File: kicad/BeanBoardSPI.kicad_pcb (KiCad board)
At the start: 4 copper layers, 199.4 x 80 mm, 42 parts, among them J1 Conn_01x16_Pin, J10 SPI1, J11 SPI2, J12 SPI3, J13 SPI4, J14 SPI5, J15 SPI6, J2 Conn_01x16_Pin, J3 Conn_01x03_Pin, J4 Conn_01x10_Pin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

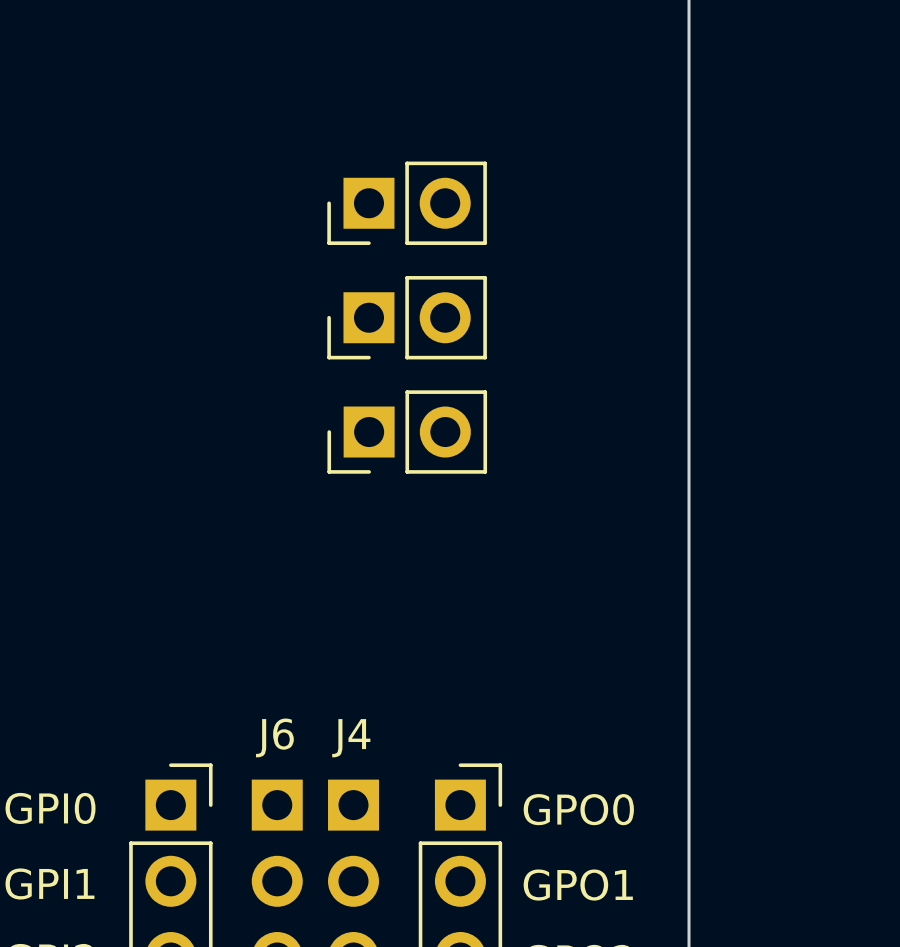
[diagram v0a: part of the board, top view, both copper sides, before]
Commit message: layout / schematic
clock divider labelling
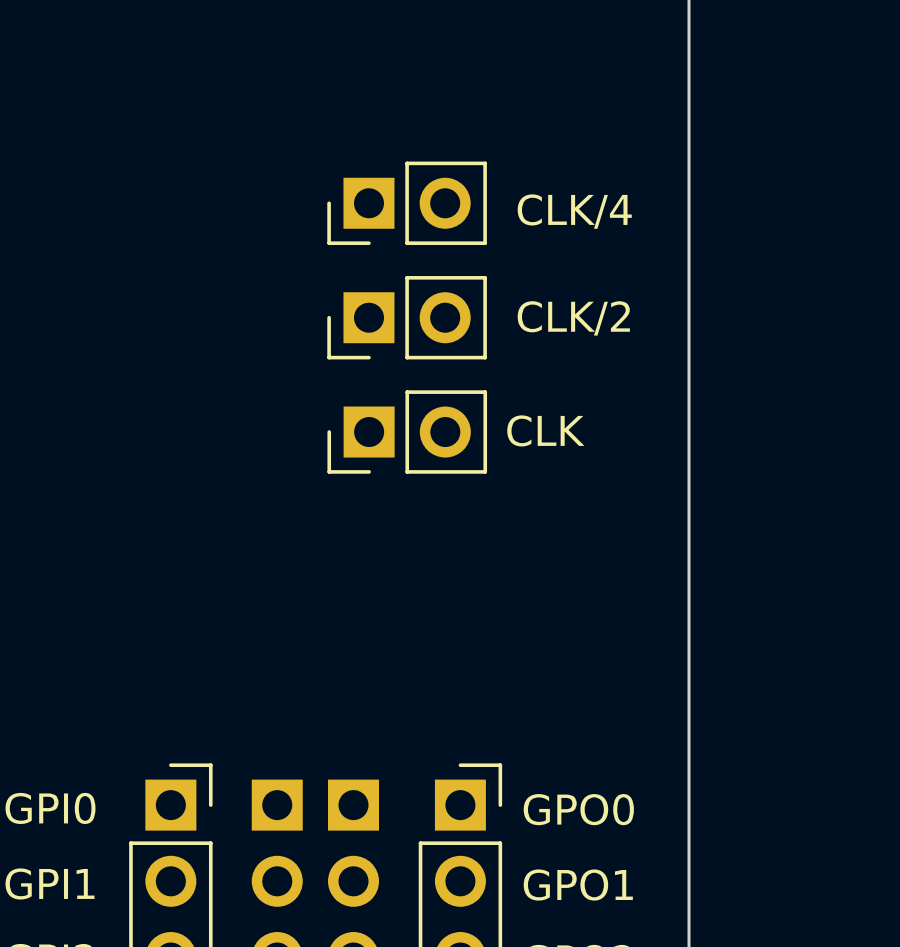
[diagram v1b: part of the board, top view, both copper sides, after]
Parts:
- JP1: value Jumper_2_Open -> CLK
- JP2: value Jumper_2_Open -> CLK/2
- JP3: value Jumper_2_Bridged -> CLK/4
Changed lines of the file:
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@@
 			)
 		)
-		(property "Value" "Jumper_2_Open"
+		(property "Value" "CLK/2"
 			(at -0.005 6.858 180)
-			(layer "F.Fab")
+			(layer "F.SilkS")
 			(effects
 				(font
@@
 		(property "Reference" "J4"
 			(at 0 -2.33 0)
-			(layer "F.SilkS")
+			(layer "F.Fab")
 			(effects
 				(font
@@
 		(property "Reference" "J6"
 			(at 0 -2.33 0)
-			(layer "F.SilkS")
+			(layer "F.Fab")
 			(effects
 				(font
@@
 			)
 		)
-		(property "Value" "Jumper_2_Open"
+		(property "Value" "CLK"
 			(at 0 5.837 180)
-			(layer "F.Fab")
+			(layer "F.SilkS")
 			(effects
 				(font
@@
 			)
 		)
-		(property "Value" "Jumper_2_Bridged"
+		(property "Value" "CLK/4"
 			(at -0.259 6.858 180)
-			(layer "F.Fab")
+			(layer "F.SilkS")
 			(effects
 				(font

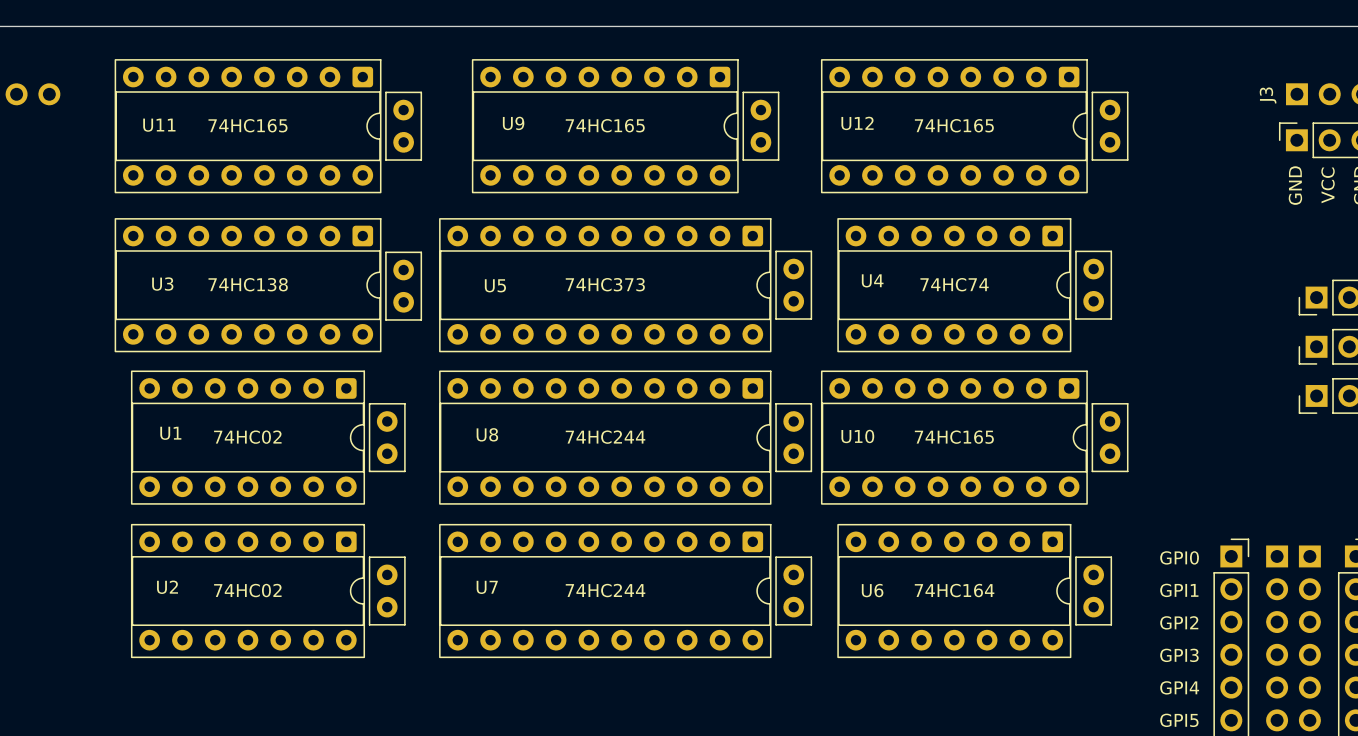
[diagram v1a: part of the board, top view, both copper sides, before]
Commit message: Update BeanBoardSPI.kicad_pcb
cap positioning
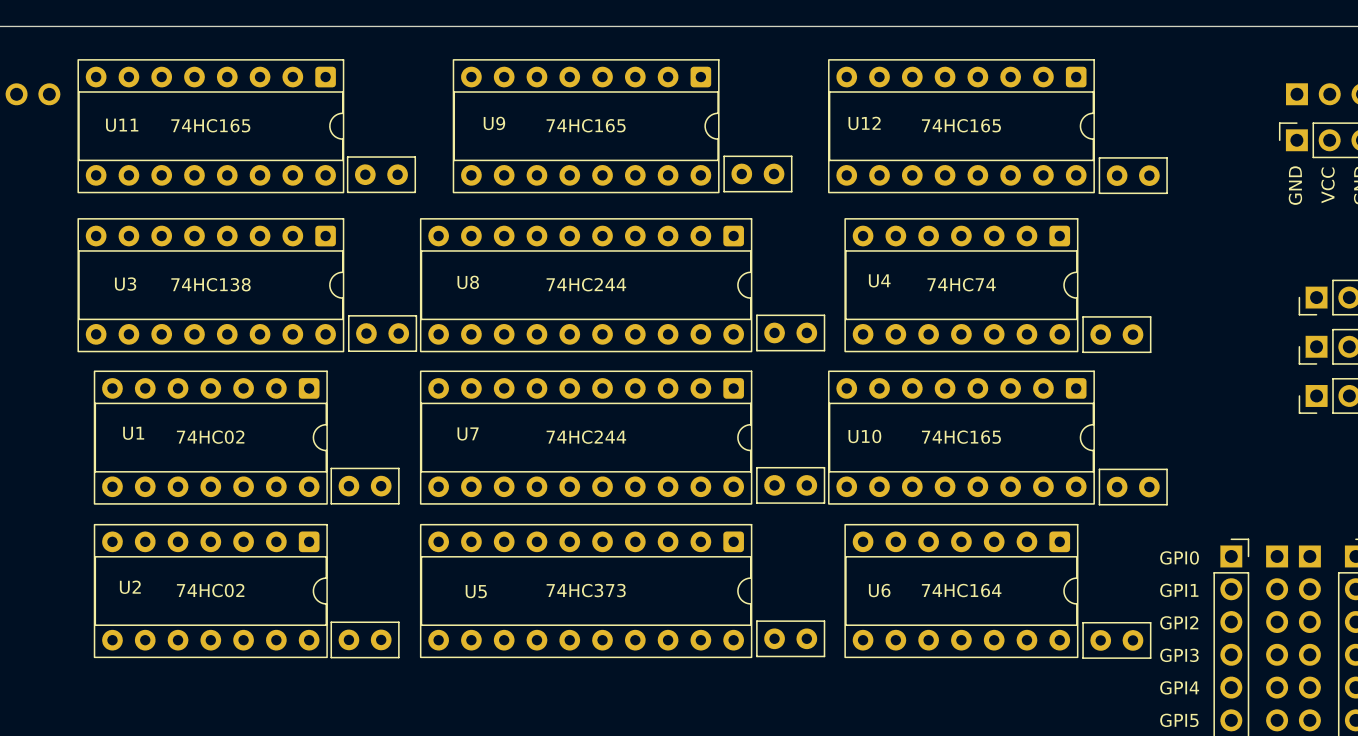
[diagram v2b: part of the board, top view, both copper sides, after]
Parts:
- moved U5 23.7 mm to (245.2, 54.7)
- moved U7 12.0 mm to (245.2, 42.8)
- moved U8 11.9 mm to (245.2, 31.0)
- moved C5 5.82 mm to (216.6, 26.2), turned to 0 degrees
- moved C6 5.70 mm to (216.7, 38.5), turned to 0 degrees
- moved C3 5.17 mm to (245.8, 26.2), turned to 0 degrees
- moved C10 5.17 mm to (248.3, 50.3), turned to 0 degrees
- moved C4 5.17 mm to (248.3, 62.2), turned to 0 degrees
- moved C9 5.17 mm to (248.3, 38.5), turned to 0 degrees
- moved C2 5.11 mm to (274.9, 50.4), turned to 0 degrees
- moved C7 5.11 mm to (273.6, 38.6), turned to 0 degrees
- moved C1 5.11 mm to (274.9, 26.3), turned to 0 degrees
- moved C8 5.11 mm to (273.6, 62.3), turned to 0 degrees
- moved U1 2.88 mm to (212.3, 42.8)
- moved U11 2.88 mm to (213.5, 18.7)
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
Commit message: Update BeanBoardSPI.kicad_pcb
tracks - data
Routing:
- net /D5: track 0.00 -> 109.5 mm, vias 0 -> 2
- net /D7: track 0.00 -> 104.9 mm, vias 0 -> 2
- net /D6: track 0.00 -> 102.5 mm, vias 0 -> 2
- net /D3: track 0.00 -> 97.6 mm, vias 0 -> 2
- net /D1: track 0.00 -> 89.5 mm, vias 0 -> 1
- net /D2: track 0.00 -> 86.0 mm
- net /D4: track 0.00 -> 74.1 mm
- net Net-(J4-Pin_9): track 0.00 -> 3.56 mm
- net Net-(J4-Pin_8): track 0.00 -> 3.56 mm
- net Net-(J4-Pin_7): track 0.00 -> 3.56 mm
- net Net-(J4-Pin_6): track 0.00 -> 3.56 mm
- net Net-(J4-Pin_5): track 0.00 -> 3.56 mm
- net Net-(J4-Pin_4): track 0.00 -> 3.56 mm
- net Net-(J4-Pin_3): track 0.00 -> 3.56 mm
- net Net-(J4-Pin_2): track 0.00 -> 3.56 mm
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
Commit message: Update BeanBoardSPI.kicad_pcb
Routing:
- net /D0: track 0.00 -> 119.7 mm, vias 0 -> 1
- net Net-(U6-Q6): track 0.00 -> 64.0 mm, vias 0 -> 1
- net Net-(U6-Q7): track 0.00 -> 61.7 mm, vias 0 -> 1
- net Net-(U6-Q5): track 0.00 -> 40.1 mm, vias 0 -> 1
- net Net-(U6-Q3): track 0.00 -> 39.6 mm, vias 0 -> 1
- net Net-(U6-Q2): track 0.00 -> 37.5 mm, vias 0 -> 1
- net Net-(U6-Q1): track 0.00 -> 35.3 mm, vias 0 -> 1
- net Net-(U6-Q0): track 0.00 -> 33.2 mm, vias 0 -> 1
- net Net-(U6-Q4): track 0.00 -> 32.9 mm, vias 0 -> 1

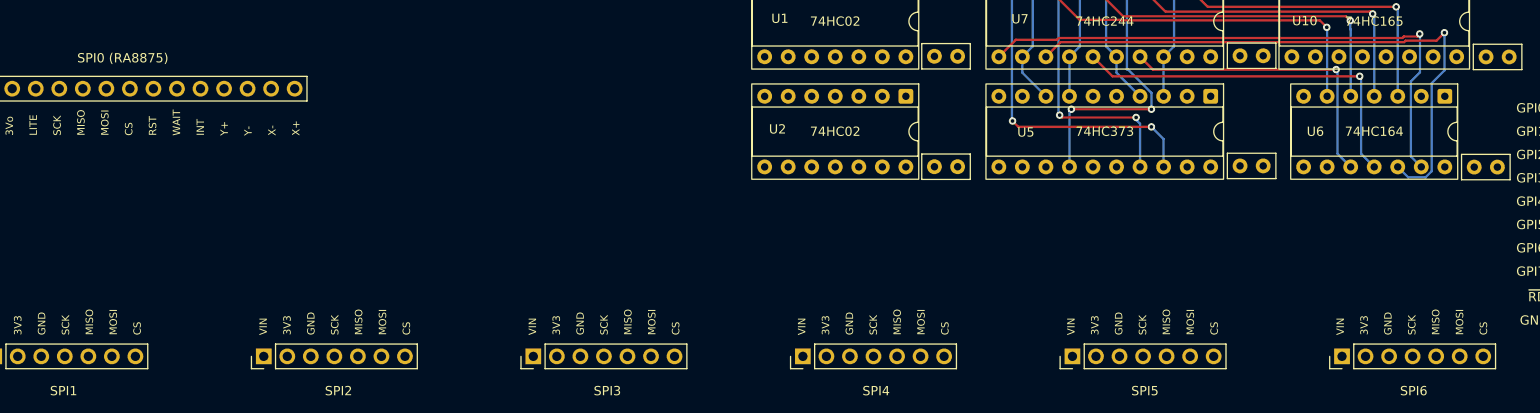
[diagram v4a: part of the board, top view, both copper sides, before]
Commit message: Update BeanBoardSPI.kicad_pcb
data / ser data tracks
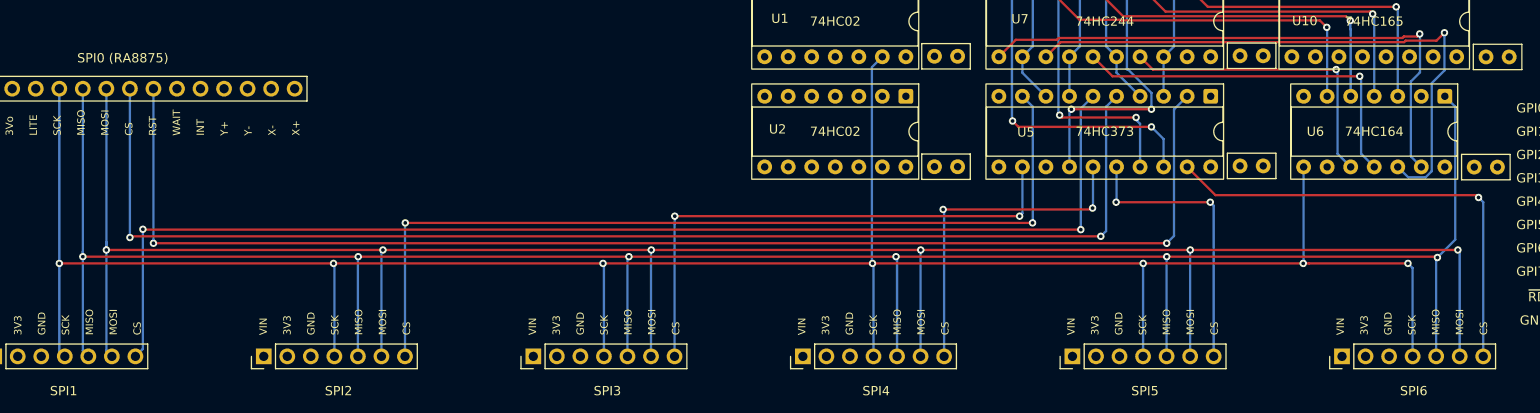
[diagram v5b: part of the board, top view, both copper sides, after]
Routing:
- net /SER_CLK: track 0.00 -> 258.4 mm, vias 0 -> 7
- net /SER_IN: track 0.00 -> 248.4 mm, vias 0 -> 6
- net /SER_OUT: track 0.00 -> 233.5 mm, vias 0 -> 6
- net /~{SRESET}: track 0.00 -> 142.8 mm, vias 0 -> 2
- net /~{CS_0}: track 0.00 -> 136.7 mm, vias 0 -> 2
- net /~{CS_1}: track 0.00 -> 130.2 mm, vias 0 -> 2
- net /~{CS_2}: track 0.00 -> 96.2 mm, vias 0 -> 2
- net /~{CS_3}: track 0.00 -> 57.8 mm, vias 0 -> 2
- net /~{CS_6}: track 0.00 -> 50.2 mm, vias 0 -> 1
- net /~{CS_4}: track 0.00 -> 36.6 mm, vias 0 -> 2
- net /~{CS_5}: track 0.00 -> 30.8 mm, vias 0 -> 2

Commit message: Update BeanBoardSPI.kicad_pcb
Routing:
- net /~{DATA_WR}: track 0.00 -> 167.1 mm, vias 0 -> 2
- net /INT_CLK: track 0.01 -> 153.1 mm
- net /DATA_WR: track 0.00 -> 139.5 mm, vias 0 -> 1
- net /CLK: track 0.00 -> 135.5 mm
- net /SER_EN: track 0.00 -> 101.9 mm, vias 0 -> 2
- net /~{SER_EN}: track 0.00 -> 100.0 mm, vias 0 -> 2
- net /~{RD}: track 0.00 -> 83.2 mm, vias 0 -> 1
- net /A3: track 0.00 -> 83.0 mm, vias 0 -> 1
- net /A2: track 0.00 -> 82.4 mm, vias 0 -> 1
- net /A1: track 0.00 -> 81.5 mm, vias 0 -> 1
- net /~{WR}: track 0.00 -> 66.0 mm, vias 0 -> 1
- net Net-(U11-DS): track 0.00 -> 58.2 mm
- net /~{DATA_RD}: track 0.00 -> 57.8 mm, vias 0 -> 1
- net Net-(U10-Q7): track 0.00 -> 57.3 mm, vias 0 -> 2
- net /~{STATUS_RD}: track 0.00 -> 53.9 mm, vias 0 -> 2
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
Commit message: Update BeanBoardSPI.kicad_pcb
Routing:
- net /D4: track 74.1 -> 118.8 mm, vias 0 -> 2
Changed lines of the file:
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@@
+	)
+	(segment
+		(start 227.375745 62.287314)
+		(end 230.460745 59.202314)
+		(width 0.25)
+		(layer "F.Cu")
+		(net "/D4")
+	)
+	(segment
+		(start 230.460745 59.202314)
+		(end 245.528745 59.202314)
+		(width 0.25)
+		(layer "F.Cu")
+		(net "/D4")
+	)
+	(segment
+		(start 241.434545 41.422314)
+		(end 240.075745 42.781114)
+		(width 0.25)
+		(layer "F.Cu")
+		(net "/D4")
 	)
 	(segment
@@
 	)
 	(segment
+		(start 246.253745 41.422314)
+		(end 241.434545 41.422314)
+		(width 0.25)
+		(layer "F.Cu")
+		(net "/D4")
+	)
+	(segment
 		(start 237.535745 26.271114)
 		(end 233.329037 22.064406)
 		(width 0.25)
 		(layer "F.Cu")
+		(net "/D4")
+	)
+	(segment
+		(start 245.528745 59.202314)
+		(end 246.761745 57.969314)
+		(width 0.25)
+		(layer "F.Cu")
+		(net "/D4")
+	)
+	(via
+		(at 246.761745 57.969314)
+		(size 0.8)
+		(drill 0.4)
+		(layers "F.Cu" "B.Cu")
+		(net "/D4")
+	)
+	(via
+		(at 246.253745 41.422314)
+		(size 0.8)
+		(drill 0.4)
+		(layers "F.Cu" "B.Cu")
 		(net "/D4")
 	)
@@
 	)
 	(segment
+		(start 246.761745 57.969314)
+		(end 246.761745 41.930314)
+		(width 0.25)
+		(layer "B.Cu")
+		(net "/D4")
+	)
+	(segment
 		(start 238.950745 41.656114)
 		(end 240.075745 42.781114)
@@
 		(width 0.25)
 		(layer "B.Cu")
+		(net "/D4")
+	)
+	(segment
+		(start 246.761745 41.930314)
+		(end 246.253745 41.422314)
+		(width 0.25)
+		(layer "B.Cu")

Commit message: Update BeanBoardSPI.kicad_pcb
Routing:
- net Net-(U2-Pad1): track 0.00 -> 15.1 mm
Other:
- board text added: "B"
- board text removed: "2"
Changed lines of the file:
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@@
 		)
 	)
-	(gr_text "2"
-		(at 296.418745 92.386314 0)
-		(layer "F.SilkS")
+	(gr_text "B"
+		(at 296.545745 92.259314 0)
+		(layer "F.SilkS" knockout)
 		(effects
 			(font
-				(size 2 2)
-				(thickness 0.375)
+				(size 1.5 1.5)
 			)
 			(justify left bottom)
@@
 	)
 	(gr_text "PainfulDiodes BeanBoardSPI"
-		(at 231.648745 92.386314 0)
+		(at 229.362745 92.386314 0)
 		(layer "F.SilkS")
 		(effects
@@
 	)
 	(segment
-		(start 120.904 82.14012)
-		(end 121.498194 82.734314)
-		(width 0.25)
-		(layer "B.Cu")
-		(net "/SER_CLK")
-	)
-	(segment
 		(start 120.904 53.848)
 		(end 120.904 82.14012)
@@
 	)
 	(segment
+		(start 120.904 82.14012)
+		(end 121.498194 82.734314)
+		(width 0.25)
+		(layer "B.Cu")
+		(net "/SER_CLK")
+	)
+	(segment
 		(start 266.446745 72.701314)
 		(end 266.949745 73.204314)
@@
 	)
 	(segment
+		(start 123.444 71.431314)
+		(end 123.444 82.14012)
+		(width 0.25)
+		(layer "B.Cu")
+		(net "/SER_IN")
+	)
+	(segment
 		(start 269.621745 72.066314)
 		(end 269.489745 72.198314)
@@
 	)
 	(segment
+		(start 123.444 82.14012)
+		(end 124.038194 82.734314)
+		(width 0.25)
+		(layer "B.Cu")
+		(net "/SER_IN")
+	)
+	(segment
 		(start 211.309124 82.734314)
 		(end 211.309124 72.083693)
@@
 	)
 	(segment
-		(start 123.444 71.431314)
-		(end 123.444 82.14012)
-		(width 0.25)
-		(layer "B.Cu")
-		(net "/SER_IN")
-	)
-	(segment
 		(start 271.548745 55.792314)
 		(end 270.423745 54.667314)
@@
 	)
 	(segment
-		(start 123.444 82.14012)
-		(end 124.038194 82.734314)
-		(width 0.25)
-		(layer "B.Cu")
-		(net "/SER_IN")
-	)
-	(segment
 		(start 182.218814 72.130245)
 		(end 182.372745 71.976314)
@@
 	)
 	(segment
+		(start 125.984 81.972314)
+		(end 126.619745 82.608059)
+		(width 0.25)
+		(layer "B.Cu")
+		(net "/SER_OUT")
+	)
+	(segment
 		(start 155.668504 71.412555)
 		(end 155.829745 71.251314)
@@
 	)
 	(segment
+		(start 126.619745 82.692763)
+		(end 126.578194 82.734314)
+		(width 0.25)
+		(layer "B.Cu")
+		(net "/SER_OUT")
+	)
+	(segment
 		(start 213.849124 82.734314)
 		(end 213.849124 71.270935)
@@
 	)
 	(segment
-		(start 242.939434 71.263625)
-		(end 242.951745 71.251314)
+		(start 126.619745 82.608059)
+		(end 126.619745 82.692763)
 		(width 0.25)
 		(layer "B.Cu")
@@
 	)
 	(segment
-		(start 184.758814 82.734314)
-		(end 184.758814 71.278245)
+		(start 242.939434 71.263625)
+		(end 242.951745 71.251314)
 		(width 0.25)
 		(layer "B.Cu")
@@
 	)
 	(segment
-		(start 125.984 70.415314)
-		(end 125.984 82.14012)
+		(start 184.758814 82.734314)
+		(end 184.758814 71.278245)
 		(width 0.25)
 		(layer "B.Cu")
@@
 	)
 	(segment
-		(start 125.984 82.14012)
-		(end 126.578194 82.734314)
+		(start 125.984 70.415314)
+		(end 125.984 81.972314)
 		(width 0.25)
 		(layer "B.Cu")
@@
 	)
 	(segment
-		(start 208.597745 53.542314)
-		(end 209.722745 54.667314)
+		(start 187.452745 53.016314)
+		(end 208.071745 53.016314)
 		(width 0.25)
 		(layer "F.Cu")
@@
 	)
 	(segment
-		(start 186.944745 53.524314)
-		(end 186.962745 53.542314)
+		(start 208.071745 53.016314)
+		(end 209.722745 54.667314)
 		(width 0.25)
 		(layer "F.Cu")
@@
 	)
 	(segment
-		(start 186.962745 53.542314)
-		(end 208.597745 53.542314)
+		(start 186.944745 53.524314)
+		(end 187.452745 53.016314)
 		(width 0.25)
 		(layer "F.Cu")
@@
 	)
 	(segment
+		(start 203.227745 53.542314)
+		(end 205.398736 53.542314)
+		(width 0.25)
+		(layer "F.Cu")
+		(net "Net-(U2-Pad1)")
+	)
+	(segment
+		(start 206.057745 55.133305)
+		(end 206.716754 55.792314)
+		(width 0.25)
+		(layer "F.Cu")
+		(net "Net-(U2-Pad1)")
+	)
+	(segment
+		(start 202.102745 54.667314)
+		(end 203.227745 53.542314)
+		(width 0.25)
+		(layer "F.Cu")
+		(net "Net-(U2-Pad1)")
+	)
+	(segment
+		(start 205.398736 53.542314)
+		(end 206.057745 54.201323)
+		(width 0.25)
+		(layer "F.Cu")
+		(net "Net-(U2-Pad1)")
+	)
+	(segment
+		(start 206.716754 55.792314)
+		(end 211.137745 55.792314)
+		(width 0.25)
+		(layer "F.Cu")
+		(net "Net-(U2-Pad1)")
+	)
+	(segment
+		(start 206.057745 54.201323)
+		(end 206.057745 55.133305)
+		(width 0.25)
+		(layer "F.Cu")
+		(net "Net-(U2-Pad1)")
+	)
+	(segment
+		(start 211.137745 55.792314)
+		(end 212.262745 54.667314)
+		(width 0.25)
+		(layer "F.Cu")
+		(net "Net-(U2-Pad1)")
+	)
+	(segment
+		(start 199.562745 54.667314)
+		(end 202.102745 54.667314)
+		(width 0.25)
+		(layer "F.Cu")
+		(net "Net-(U2-Pad1)")
+	)
+	(segment
